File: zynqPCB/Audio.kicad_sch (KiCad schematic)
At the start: 67 parts, among them J5 AUDIO JACK, J6 AUDIO JACK, J7 AUDIO JACK, J8 JACK_TRS_4PINS, Q10 IRLML2502, Q5 IRLML2502, Q6 IRLML2502, Q7 IRLML2502, Q8 IRLML2502, Q9 IRLML2502, U20 xc7z020clg484, U21 TLV320AIC3104

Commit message: Sensores Removed
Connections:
- net IMU_INT1: no longer names the net of U20.W15 (IO_L21P_T3_DQS_33)
- net IMU_INT2: no longer names the net of U20.Y15 (IO_L21N_T3_DQS_33)
- net IR_RX: no longer names the net of U20.AA18 (IO_L12N_T1_MRCC_33)
- net TEMPO_SW: no longer names the net of U20.Y14 (IO_L22P_T3_33)
- no-connect marks 19 -> 23
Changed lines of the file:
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@@
+	)
+	(no_connect
+		(at 50.8 74.93)
 	)
 	(no_connect
@@
 	)
 	(no_connect
+		(at 50.8 128.27)
+	)
+	(no_connect
 		(at 50.8 115.57)
 	)
@@
 	)
 	(no_connect
+		(at 50.8 123.19)
+	)
+	(no_connect
 		(at 50.8 92.71)
 	)
@@
 	(no_connect
 		(at 50.8 77.47)
+	)
+	(no_connect
+		(at 50.8 120.65)
 	)
 	(no_connect
@@
 		)
 	)
-	(global_label "TEMPO_SW"
-		(shape input)
-		(at 50.8 128.27 0)
-		(effects
-			(font
-				(size 1.524 1.524)
-			)
-			(justify left)
-		)
-		(property "Intersheetrefs" "${INTERSHEET_REFS}"
-			(at 50.8 128.27 0)
-			(effects
-				(font
-					(size 1.27 1.27)
-				)
-				(hide yes)
-			)
-		)
-	)
 	(global_label "JD_LOUT"
 		(shape input)
@@
 		)
 	)
-	(global_label "IMU_INT2"
-		(shape input)
-		(at 50.8 120.65 0)
-		(effects
-			(font
-				(size 1.524 1.524)
-			)
-			(justify left)
-		)
-		(property "Intersheetrefs" "${INTERSHEET_REFS}"
-			(at 50.8 120.65 0)
-			(effects
-				(font
-					(size 1.27 1.27)
-				)
-				(hide yes)
-			)
-		)
-	)
 	(global_label "I2C33_SCLK"
 		(shape input)
@@
 		)
 	)
-	(global_label "IMU_INT1"
-		(shape input)
-		(at 50.8 123.19 0)
-		(effects
-			(font
-				(size 1.524 1.524)
-			)
-			(justify left)
-		)
-		(property "Intersheetrefs" "${INTERSHEET_REFS}"
-			(at 50.8 123.19 0)
-			(effects
-				(font
-					(size 1.27 1.27)
-				)
-				(hide yes)
-			)
-		)
-	)
 	(global_label "I2S_BCLK"
 		(shape output)
@@
 			(effects
 				(font
-					(size 1.27 1.27)
-				)
-				(hide yes)
-			)
-		)
-	)
-	(global_label "IR_RX"
-		(shape input)
-		(at 50.8 74.93 0)
-		(effects
-			(font
-				(size 1.524 1.524)
-			)
-			(justify left)
-		)
-		(property "Intersheetrefs" "${INTERSHEET_REFS}"
-			(at 50.8 74.93 0)
-			(effects
-				(font

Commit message: update audio
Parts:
- removed C107: 2.2uF, Capacitor_SMD:C_0402_1005Metric, symbol Device:C
- removed C108, C111, C121, C122, C124, C127, C128, C129: .1uF, Capacitor_SMD:C_0402_1005Metric, symbol Device:C
- removed C109, C110, C112, C117: 1uF, Capacitor_SMD:C_0402_1005Metric, symbol Device:C
- removed C113, C120, C123, C125, C126: 10uF, Capacitor_SMD:C_0603_1608Metric, symbol Device:C
- removed C114: 4.7uF, Capacitor_SMD:C_0402_1005Metric, symbol Device:C_Small
- removed C118, C119: 220uF Tant., Capacitor_Tantalum_SMD:CP_EIA-3528-12_Kemet-T, symbol Device:CP1_Small
- removed J5, J6, J7: AUDIO JACK, DFTcustom:RA49C14B, symbol DFTBoard-rescue:JACK_TRS_5PINS
- removed J8: JACK_TRS_4PINS, DFTcustom:SJ-352X-SMT, symbol DFTBoard-rescue:JACK_TRS_4PINS
- removed MIC1: MEMSMIC, SPW2430HR5H-B:MIC_SPW2430HR5H-B, symbol DFTBoard-rescue:MEMSMIC
- removed R100: 1k, Resistor_SMD:R_0402_1005Metric, symbol Device:R_Small
- removed R101, R102, R103, R92: 100k, Resistor_SMD:R_0402_1005Metric, symbol Device:R
- removed R104, R105, R106, R93: 49.9k, Resistor_SMD:R_0402_1005Metric, symbol Device:R
- removed U21: TLV320AIC3104, Package_DFN_QFN:QFN-32-1EP_5x5mm_P0.5mm_EP3.65x3.65mm, symbol DFTBoard-rescue:TLV320AIC3104
- added R1, R2, R29, R3, R4, R5: R, symbol DFTCustom:R
- added R6: R, symbol Device:R
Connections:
- net GND: now also R1.2, R2.2, R29.2, R3.2, R4.2, R5.2, R6.2
- net I2S_BCLK: no longer U20.AA13 (IO_L23N_T3_33)
- net I2S_LRCLK: no longer U20.AB14 (IO_L24P_T3_33)
- net I2S_ADCSD: no longer names the net of U20.AB15 (IO_L24N_T3_33)
- net I2S_ADCSD: now also R5.1
- net I2S_DACSD: no longer names the net of U20.AA14 (IO_L22N_T3_33)
- net I2S_MCLK: no longer names the net of U20.Y13 (IO_L23P_T3_33)
- net JD_HOUT: no longer names the net of U20.AB17 (IO_L17N_T2_33)
- net JD_HOUT: now also R2.1
- net JD_IN: no longer names the net of U20.W17 (IO_L13P_T2_MRCC_33)
- net JD_IN: now also R1.1
- net JD_LOUT: no longer names the net of U20.AB16 (IO_L18N_T2_33)
- net JD_LOUT: now also R3.1
- net JD_ROUT: no longer names the net of U20.AB19 (IO_L10P_T1_33)
- net JD_ROUT: now also R4.1
- net TLV_RST#: no longer names the net of U20.AA17 (IO_L17P_T2_33)
- new net: R29.1, U20.AA13 (IO_L23N_T3_33)
- new net: R6.1, U20.AB14 (IO_L24P_T3_33)
- no-connect marks 23 -> 27
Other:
- note added: "Considering Master was Codec , So will gnd fgpa corresponding pins,Safer option ,Disadvantge two pin used"
- note added: "Grounded or 3.3V so that no jack is connected assured,depend on systm for now it is grounded(W17)"
- note removed: "Anticipate 1V Pk-Pk"
- moved on the sheet: C100, C101, C102, C103, C104, C105, C106

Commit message: removed grounded resistor can configure from the vivado and removed LCD
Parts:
- removed R1, R2, R29, R3, R4, R5: R, symbol DFTCustom:R
- removed R6: R, symbol Device:R
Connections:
- no-connect marks 27 -> 34

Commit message: Audio removed
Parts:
- removed C115, C116: 1uF, Capacitor_SMD:C_0402_1005Metric, symbol Device:C
- removed D6, D7: LED_RGB, DFTcustom:PLCC6-SM-RGB-LED, symbol DFTBoard-rescue:LED_RGB-RESCUE-DFTBoard-
- removed GT1: GNDTIE, DFTcustom:gndtie, symbol DFTBoard-rescue:GNDTIE-
- removed Q10, Q5, Q6, Q7, Q8, Q9: IRLML2502, Package_TO_SOT_SMD:SOT-23, symbol DFTBoard-rescue:IRLML2502-
- removed R86, R87, R88, R89, R90, R91, R95, R96, R98, R99: 100, Resistor_SMD:R_0402_1005Metric, symbol Device:R
- removed R94, R97: 150, Resistor_SMD:R_0402_1005Metric, symbol Device:R
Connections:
- net LCD_D0: no longer names the net of U20.AB21 (IO_L8N_T1_33)
- net LCD_D1: no longer names the net of U20.AB22 (IO_L7N_T1_33)
- net LCD_D10: no longer names the net of U20.U20 (IO_L5P_T0_33)
- net LCD_D11: no longer names the net of U20.AA21 (IO_L8P_T1_33)
- net LCD_D12: no longer names the net of U20.AA22 (IO_L7P_T1_33)
- net LCD_D13: no longer names the net of U20.Y21 (IO_L9N_T1_DQS_33)
- net LCD_D14: no longer names the net of U20.Y20 (IO_L9P_T1_DQS_33)
- net LCD_D15: no longer names the net of U20.W22 (IO_L3N_T0_DQS_33)
- net LCD_D16: no longer names the net of U20.W21 (IO_L4N_T0_33)
- net LCD_D17: no longer names the net of U20.V22 (IO_L3P_T0_DQS_33)
- net LCD_D18: no longer names the net of U20.V20 (IO_L5N_T0_33)
- net LCD_D19: no longer names the net of U20.U22 (IO_L2N_T0_33)
- net LCD_D2: no longer names the net of U20.U19 (IO_0_33)
- net LCD_D20: no longer names the net of U20.U21 (IO_L1N_T0_33)
- net LCD_D21: no longer names the net of U20.T22 (IO_L2P_T0_33)
- net LCD_D22: no longer names the net of U20.T21 (IO_L1P_T0_33)
- net LCD_D3: no longer names the net of U20.W20 (IO_L4P_T0_33)
- net LED_1B_CTRL: no longer names the net of U20.Y19 (IO_L11P_T1_SRCC_33)
- net LED_1G_CTRL: no longer names the net of U20.AB20 (IO_L10N_T1_33)
- net LED_1R_CTRL: no longer names the net of U20.AA19 (IO_L11N_T1_SRCC_33)
- no-connect marks 34 -> 50
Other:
- note removed: "Audio and HDMI"

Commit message: audio capacitors
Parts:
- removed C100, C101, C102, C103: .47uF, Capacitor_SMD:C_0402_1005Metric, symbol Device:C_Small
- removed C104, C105: 4.7uF, Capacitor_SMD:C_0402_1005Metric, symbol Device:C_Small
- removed C106: 47uF, Capacitor_SMD:C_0805_2012Metric, symbol Device:C_Small

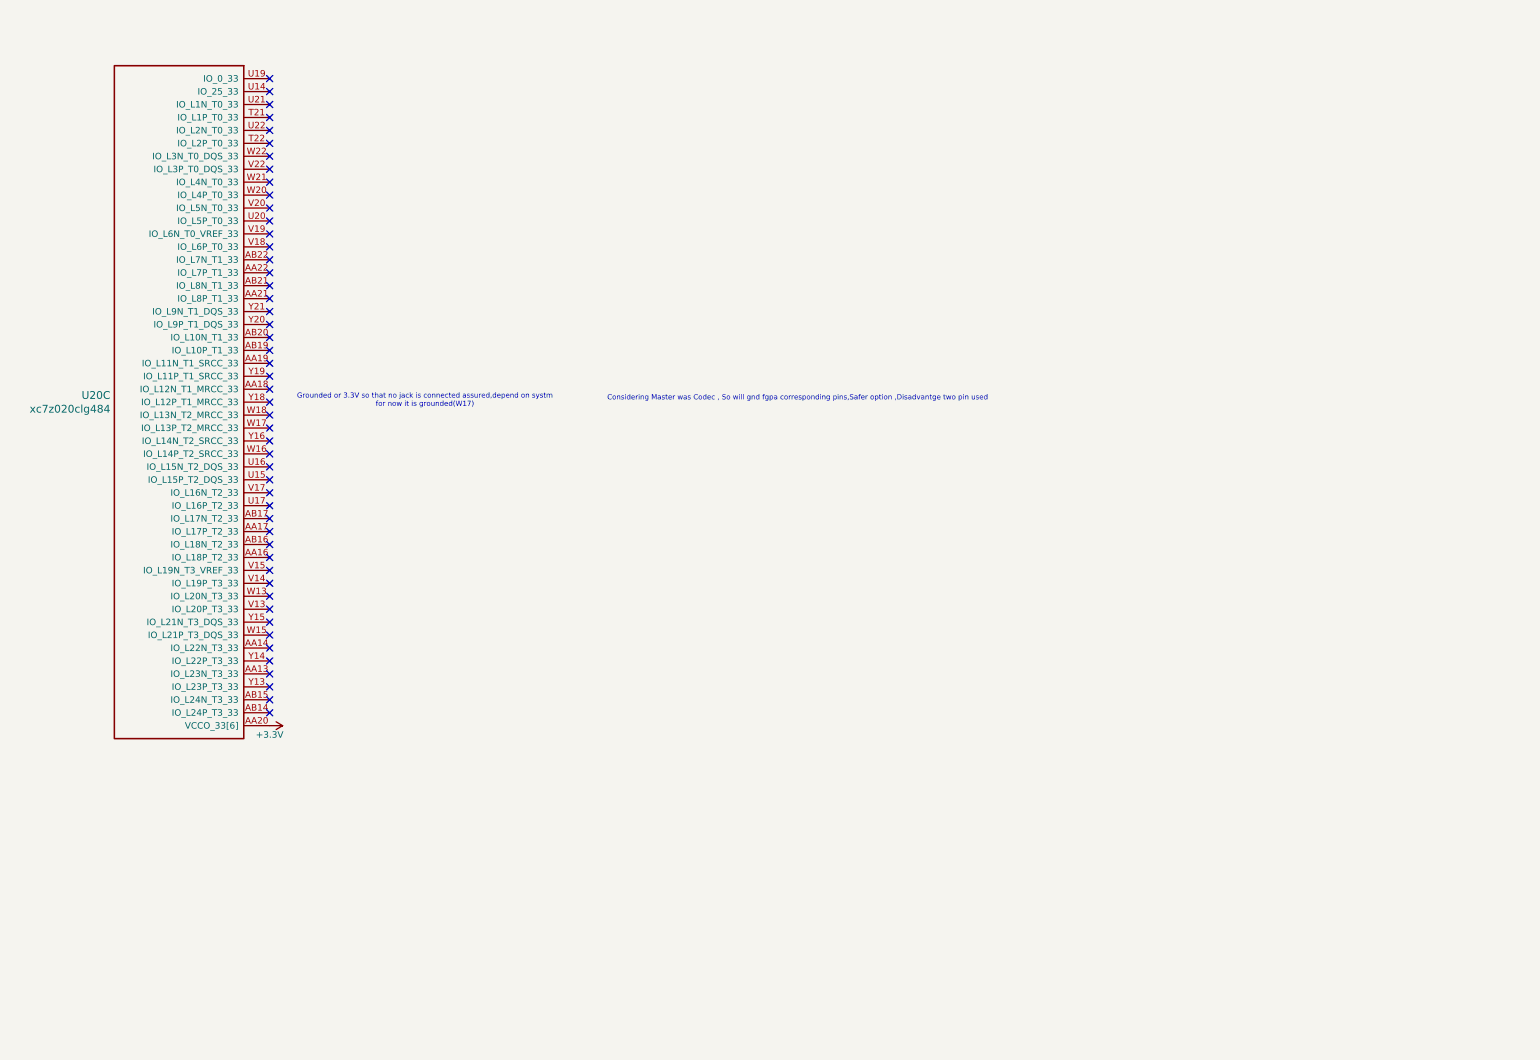
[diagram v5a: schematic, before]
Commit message: Camera added
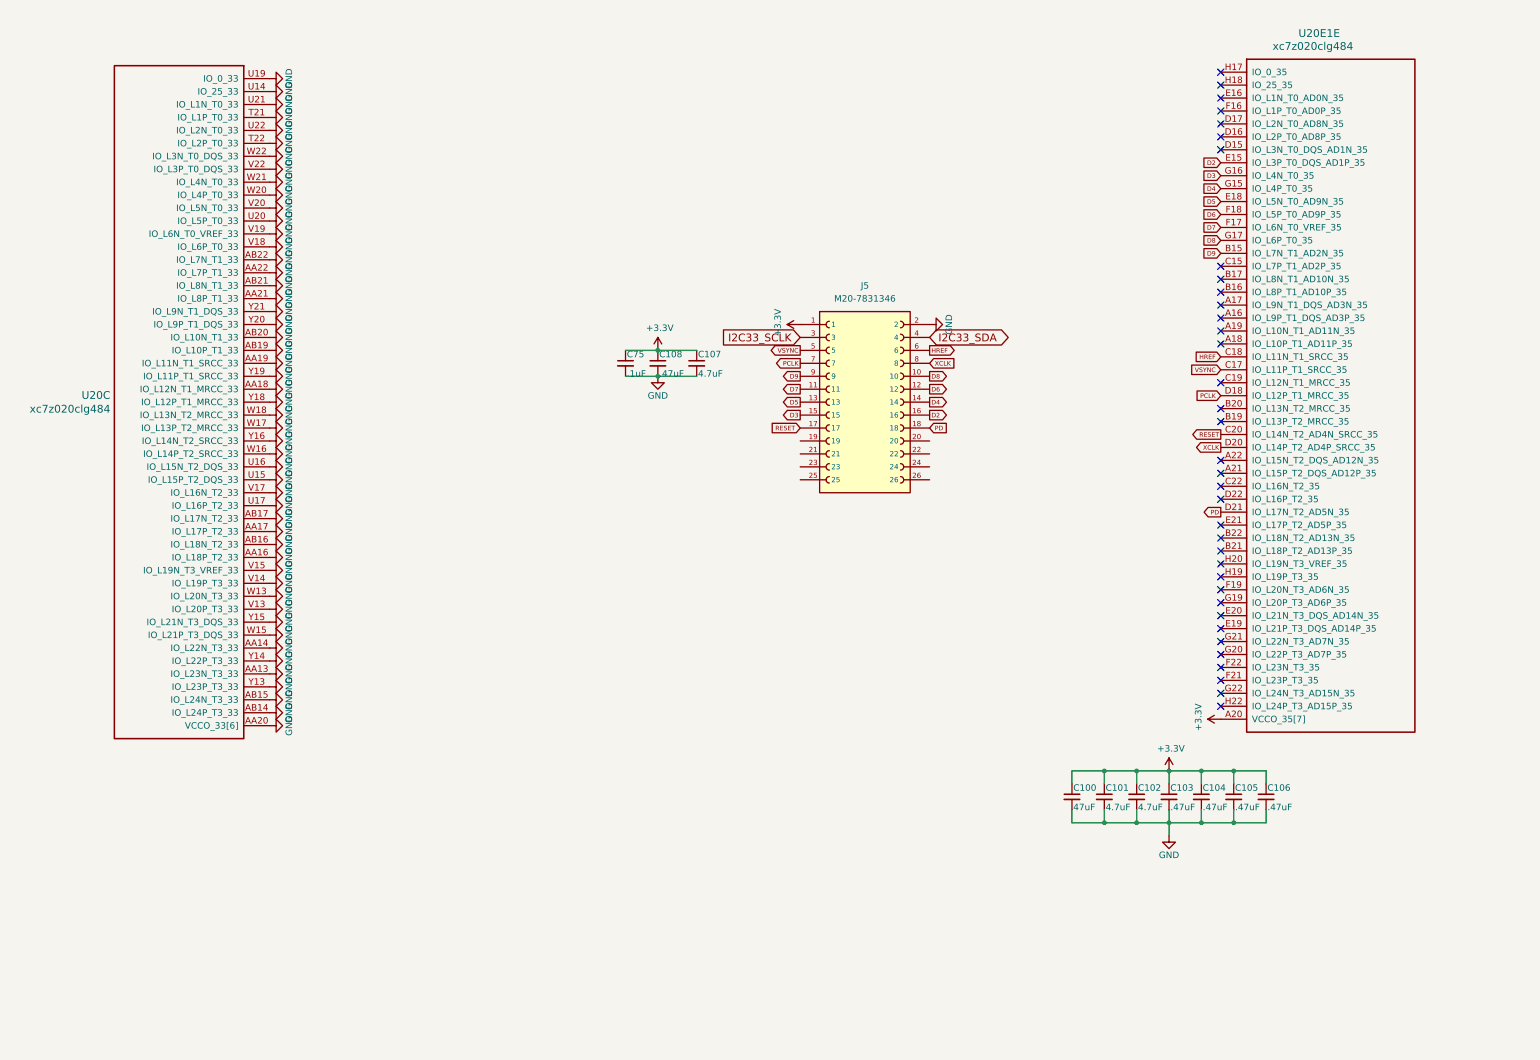
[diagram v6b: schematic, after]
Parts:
- added C100: 47uF, Capacitor_SMD:C_1210_3225Metric, symbol Device:C_Small
- added C101, C102, C107: 4.7uF, Capacitor_SMD:C_0402_1005Metric, symbol Device:C_Small
- added C103, C104, C105, C106, C108: .47uF, Capacitor_SMD:C_0402_1005Metric, symbol Device:C_Small
- added C75: .1uF, Capacitor_SMD:C_0402_1005Metric, symbol Device:C_Small
- added J5: M20-7831346, M20-7831346:HARWIN_M20-7831346, symbol M20-7831346:M20-7831346
- added U20E1: xc7z020clg484, DFTcustom:BGA-484_19.0x19.0mm_Layout22x22_P0.80mm_dia0.40mm, symbol xilinx7:xc7z020clg484
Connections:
- net +3.3V: now also C100.1, C101.1, C102.1, C103.1, C104.1, C105.1, C106.1, C107.1, C108.1, C75.1, J5.1, U20E1.A20 (VCCO_35[7]), U20E1.C16 (VCCO_35[7]), U20E1.D19 (VCCO_35[7]), U20E1.E22 (VCCO_35[7]), U20E1.F15 (VCCO_35[7]), U20E1.G18 (VCCO_35[7]), U20E1.H21 (VCCO_35[7]); no longer U20.AA20 (VCCO_33[6]), U20.AB13 (VCCO_33[6]), U20.U18 (VCCO_33[6]), U20.V21 (VCCO_33[6]), U20.W14 (VCCO_33[6]), U20.Y17 (VCCO_33[6])
- net GND: now reaches U20.AA13 (IO_L23N_T3_33)
- net GND: now also U20.AA14 (IO_L22N_T3_33), U20.AA16 (IO_L18P_T2_33), U20.AA17 (IO_L17P_T2_33), U20.AA18 (IO_L12N_T1_MRCC_33), U20.AA19 (IO_L11N_T1_SRCC_33), U20.AA20 (VCCO_33[6]), U20.AA21 (IO_L8P_T1_33), U20.AA22 (IO_L7P_T1_33), U20.AB13 (VCCO_33[6]), U20.AB14 (IO_L24P_T3_33), U20.AB15 (IO_L24N_T3_33), U20.AB16 (IO_L18N_T2_33), U20.AB17 (IO_L17N_T2_33), U20.AB19 (IO_L10P_T1_33), U20.AB20 (IO_L10N_T1_33), U20.AB21 (IO_L8N_T1_33), U20.AB22 (IO_L7N_T1_33), U20.T21 (IO_L1P_T0_33), U20.T22 (IO_L2P_T0_33), U20.U14 (IO_25_33), U20.U15 (IO_L15P_T2_DQS_33), U20.U16 (IO_L15N_T2_DQS_33), U20.U17 (IO_L16P_T2_33), U20.U18 (VCCO_33[6]), U20.U19 (IO_0_33), U20.U20 (IO_L5P_T0_33), U20.U21 (IO_L1N_T0_33), U20.U22 (IO_L2N_T0_33), U20.V13 (IO_L20P_T3_33), U20.V14 (IO_L19P_T3_33), U20.V15 (IO_L19N_T3_VREF_33), U20.V17 (IO_L16N_T2_33), U20.V18 (IO_L6P_T0_33), U20.V19 (IO_L6N_T0_VREF_33), U20.V20 (IO_L5N_T0_33), U20.V21 (VCCO_33[6]), U20.V22 (IO_L3P_T0_DQS_33), U20.W13 (IO_L20N_T3_33), U20.W14 (VCCO_33[6]), U20.W15 (IO_L21P_T3_DQS_33), U20.W16 (IO_L14P_T2_SRCC_33), U20.W17 (IO_L13P_T2_MRCC_33), U20.W18 (IO_L13N_T2_MRCC_33), U20.W20 (IO_L4P_T0_33), U20.W21 (IO_L4N_T0_33), U20.W22 (IO_L3N_T0_DQS_33), U20.Y13 (IO_L23P_T3_33), U20.Y14 (IO_L22P_T3_33), U20.Y15 (IO_L21N_T3_DQS_33), U20.Y16 (IO_L14N_T2_SRCC_33), U20.Y17 (VCCO_33[6]), U20.Y18 (IO_L12P_T1_MRCC_33), U20.Y19 (IO_L11P_T1_SRCC_33), U20.Y20 (IO_L9P_T1_DQS_33), U20.Y21 (IO_L9N_T1_DQS_33), C100.2, C101.2, C102.2, C103.2, C104.2, C105.2, C106.2, C107.2, C108.2, C75.2, J5.2
- new net D2: J5.16, U20E1.E15 (IO_L3P_T0_DQS_AD1P_35)
- new net D3: J5.15, U20E1.G16 (IO_L4N_T0_35)
- new net D4: J5.14, U20E1.G15 (IO_L4P_T0_35)
- new net D5: J5.13, U20E1.E18 (IO_L5N_T0_AD9N_35)
- new net D6: J5.12, U20E1.F18 (IO_L5P_T0_AD9P_35)
- new net D7: J5.11, U20E1.F17 (IO_L6N_T0_VREF_35)
- new net D8: J5.10, U20E1.G17 (IO_L6P_T0_35)
- new net D9: J5.9, U20E1.B15 (IO_L7N_T1_AD2N_35)
- new net HREF: J5.6, U20E1.C18 (IO_L11N_T1_SRCC_35)
- new net I2C33_SCLK: J5.3
- new net I2C33_SDA: J5.4
- new net PCLK: J5.7, U20E1.D18 (IO_L12P_T1_MRCC_35)
- new net PD: J5.18, U20E1.D21 (IO_L17N_T2_AD5N_35)
- new net RESET: J5.17, U20E1.C20 (IO_L14N_T2_AD4N_SRCC_35)
- new net VSYNC: J5.5, U20E1.C17 (IO_L11P_T1_SRCC_35)
- new net XCLK: J5.8, U20E1.D20 (IO_L14P_T2_AD4P_SRCC_35)
- no-connect marks 50 -> 36
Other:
- note removed: "Considering Master was Codec , So will gnd fgpa corresponding pins,Safer option ,Disadvantge two pin used"
- note removed: "Grounded or 3.3V so that no jack is connected assured,depend on systm for now it is grounded(W17)"
